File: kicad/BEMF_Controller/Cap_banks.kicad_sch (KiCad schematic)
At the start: 60 parts

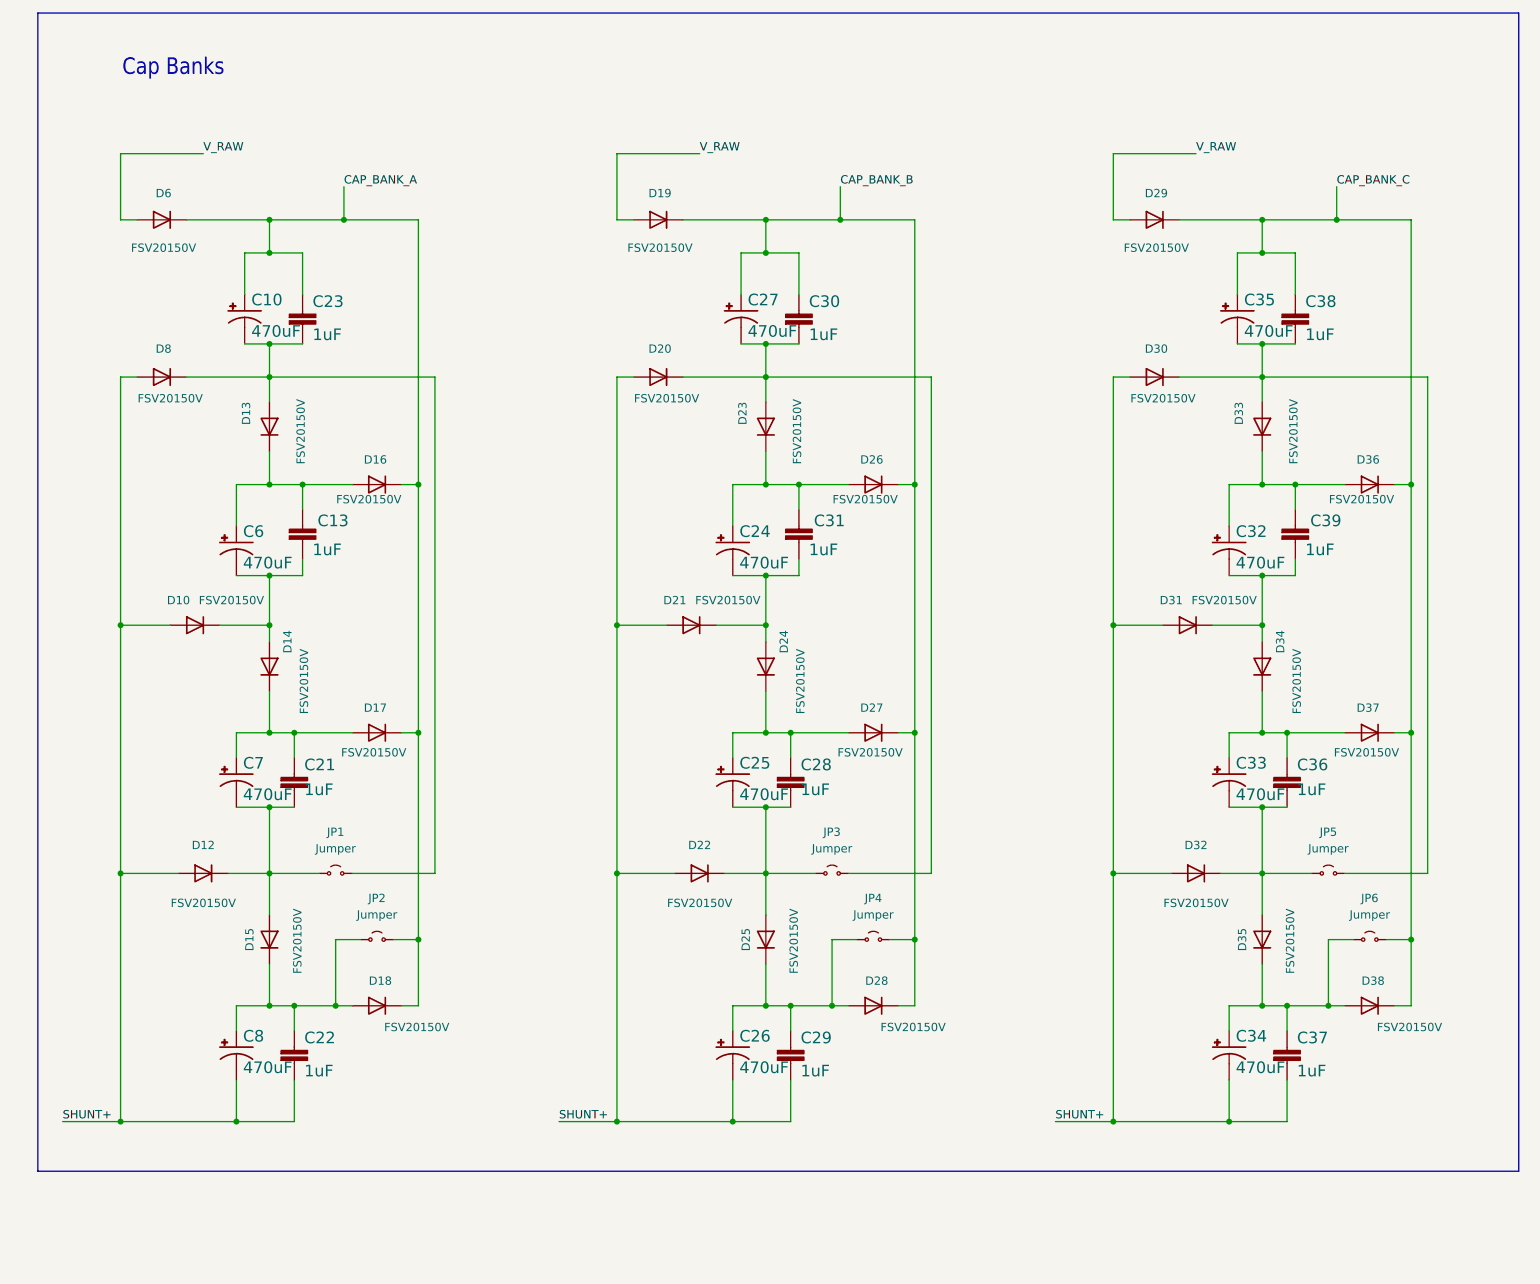
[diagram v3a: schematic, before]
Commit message: Updated Shottky footprint
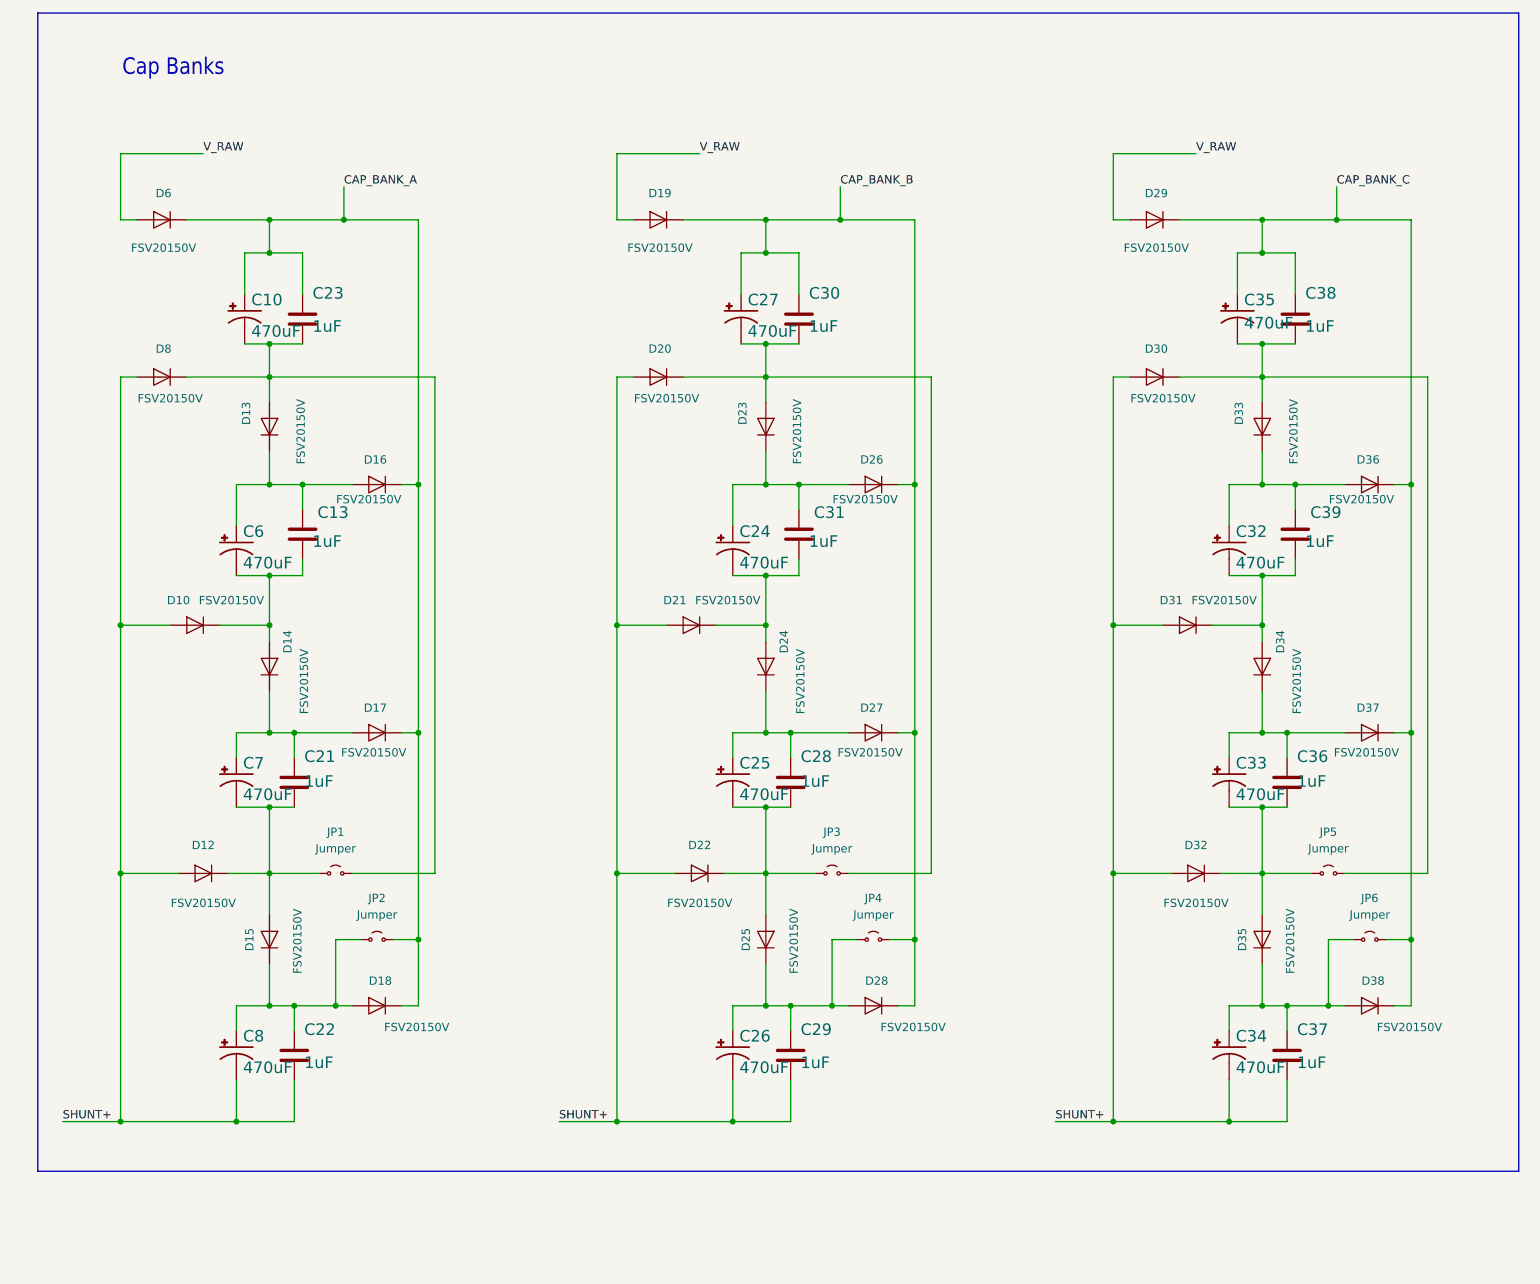
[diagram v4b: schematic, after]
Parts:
- C13, C21, C22, C23, C28, C29, C30, C31, C36, C37, C38, C39: footprint main:1206 -> Capacitor_SMD:C_1812_4532Metric; symbol main-eagle-import:1.0UF-1206-50V-10% -> Component_Library:CHV1812N250105MXT
- D10, D12, D13, D14, D15, D16, D17, D18, D19, D20, D21, D22, D23, D24, D25, D26, D27, D28, D29, D30, D31, D32, D33, D34, D35, D36, D37, D38, D6, D8: symbol Device:D -> Component_Library:FSV20150V
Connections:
- net CAP_BANK_A: now also D16.2 (A), D17.2 (A), D18.2 (A), D6.2 (A)
- net CAP_BANK_B: now also D19.2 (A), D26.2 (A), D27.2 (A), D28.2 (A)
- net CAP_BANK_C: now also D29.2 (A), D36.2 (A), D37.2 (A), D38.2 (A)
- net SHUNT+: now also D10.3 (K), D12.3 (K), D20.3 (K), D21.3 (K), D22.3 (K), D30.3 (K), D31.3 (K), D32.3 (K), D8.3 (K); no longer D10.2 (A), D12.2 (A), D20.2 (A), D21.2 (A), D22.2 (A), D30.2 (A), D31.2 (A), D32.2 (A), D8.2 (A)
- net V_RAW: now also D19.3 (K), D29.3 (K), D6.3 (K); no longer D19.2 (A), D29.2 (A), D6.2 (A)
- net at C27.-, C30.2, D20.1 (A)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: now also D20.2 (A), D23.3 (K); no longer D23.2 (A)
- net at C25.+, C28.1, D24.1 (A): now also D24.2 (A), D27.3 (K); no longer D27.2 (A)
- net at C24.-, C31.2, D21.1 (A): now also D21.2 (A), D24.3 (K); no longer D24.2 (A)
- net at C13.1, C6.+, D13.1 (A): now also D13.2 (A), D16.3 (K); no longer D16.2 (A)
- net at C34.+, C37.1, D35.1 (A)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: now also D35.2 (A), D38.3 (K); no longer D38.2 (A)
- net at C10.-, C23.2, D8.1 (A)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: now also D13.3 (K), D8.2 (A); no longer D13.2 (A)
- net at C22.1, C8.+, D15.1 (A)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: now also D15.2 (A), D18.3 (K); no longer D18.2 (A)
- net at C26.+, C29.1, D25.1 (A)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: now also D25.2 (A), D28.3 (K); no longer D28.2 (A)
- net at C25.-, C28.2, D22.1 (A)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: now also D22.2 (A), D25.3 (K); no longer D25.2 (A)
- net at C33.+, C36.1, D34.1 (A): now also D34.2 (A), D37.3 (K); no longer D37.2 (A)
- net at C33.-, C36.2, D32.1 (A)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: now also D32.2 (A), D35.3 (K); no longer D35.2 (A)
- net at C21.2, C7.-, D12.1 (A)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: now also D12.2 (A), D15.3 (K); no longer D15.2 (A)
- net at C35.-, C38.2, D30.1 (A)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: now also D30.2 (A), D33.3 (K); no longer D33.2 (A)
- net at C13.2, C6.-, D10.1 (A): now also D10.2 (A), D14.3 (K); no longer D14.2 (A)
- net at C24.+, C31.1, D23.1 (A): now also D23.2 (A), D26.3 (K); no longer D26.2 (A)
- net at C32.+, C39.1, D33.1 (A): now also D33.2 (A), D36.3 (K); no longer D36.2 (A)
- net at C21.1, C7.+, D14.1 (A): now also D14.2 (A), D17.3 (K); no longer D17.2 (A)
- net at C32.-, C39.2, D31.1 (A): now also D31.2 (A), D34.3 (K); no longer D34.2 (A)

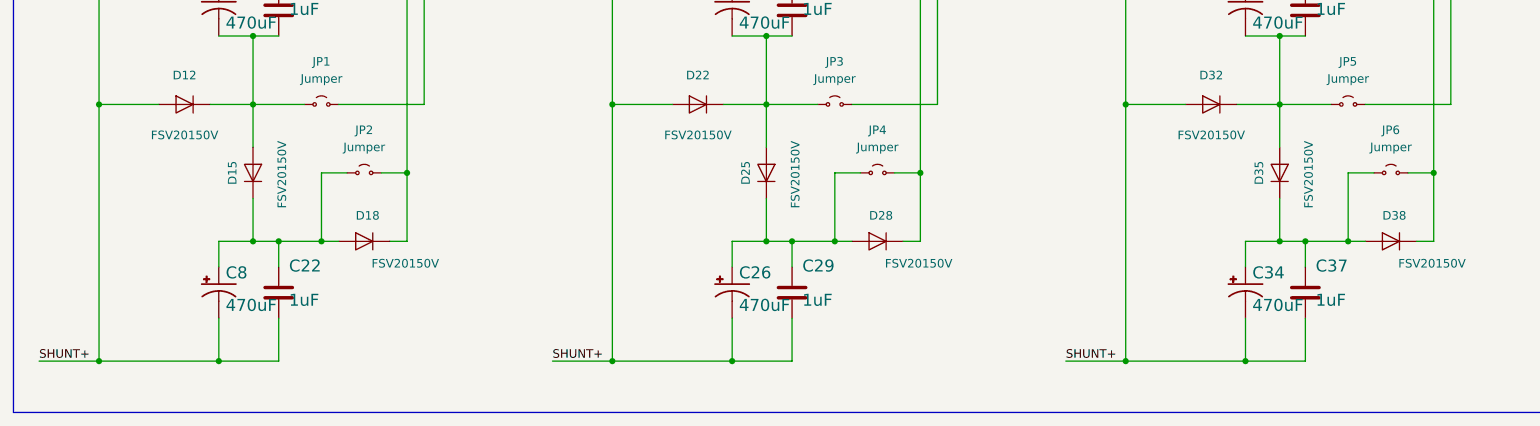
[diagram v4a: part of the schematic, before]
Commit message: Added external spi ADC for current and voltage sense per bridge
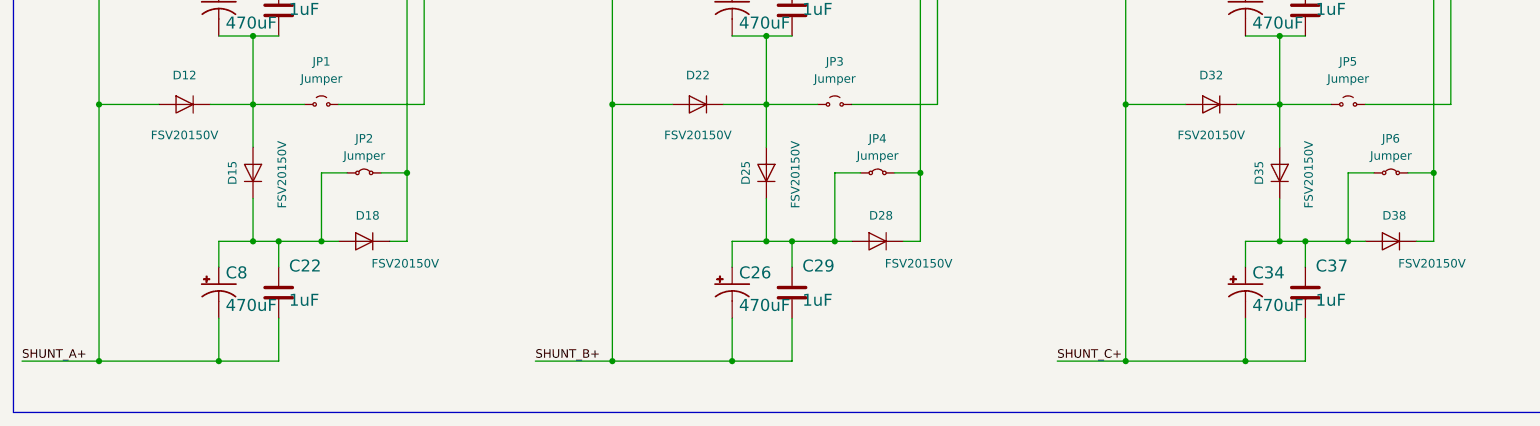
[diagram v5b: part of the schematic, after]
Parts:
- removed JP2, JP4, JP6: Jumper, Jumper:SolderJumper-2_P1.3mm_Open_RoundedPad1.0x1.5mm, symbol Jumper:Jumper_2_Small_Open
- added JP2, JP4, JP6: Jumper, Jumper:SolderJumper-2_P1.3mm_Bridged2Bar_RoundedPad1.0x1.5mm, symbol Jumper:Jumper_2_Small_Bridged
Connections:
- net CAP_BANK_A: now also JP2.2 (B)
- net CAP_BANK_B: now also JP4.2 (B)
- net CAP_BANK_C: now also JP6.2 (B)
- net at C34.+, C37.1, D35.1 (A)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: now also JP6.1 (A)
- net at C22.1, C8.+, D15.1 (A)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: now also JP2.1 (A)
- net at C26.+, C29.1, D25.1 (A)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: now also JP4.1 (A)
- removed net SHUNT+: C22.2, C26.-, C29.2, C34.-, C37.2, C8.-, D10.3 (K), D12.3 (K), D20.3 (K), D21.3 (K), D22.3 (K), D30.3 (K), D31.3 (K), D32.3 (K), D8.3 (K)
- new net SHUNT_A+: C22.2, C8.-, D10.3 (K), D12.3 (K), D8.3 (K)
- new net SHUNT_B+: C26.-, C29.2, D20.3 (K), D21.3 (K), D22.3 (K)
- new net SHUNT_C+: C34.-, C37.2, D30.3 (K), D31.3 (K), D32.3 (K)
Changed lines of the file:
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@@
 	(wire
 		(pts
-			(xy 12.7 175.26) (xy 21.59 175.26)
+			(xy 10.16 175.26) (xy 21.59 175.26)
 		)
 		(stroke
@@
 	(wire
 		(pts
-			(xy 88.9 175.26) (xy 97.79 175.26)
+			(xy 86.36 175.26) (xy 97.79 175.26)
 		)
 		(stroke
@@
 	(wire
 		(pts
-			(xy 165.1 175.26) (xy 173.99 175.26)
+			(xy 163.83 175.26) (xy 173.99 175.26)
 		)
 		(stroke
@@
 		)
 	)
-	(label "SHUNT+"
-		(at 88.9 175.26 0)
+	(label "SHUNT_B+"
+		(at 86.36 175.26 0)
 		(fields_autoplaced yes)
 		(effects
@@
 		)
 	)
-	(label "SHUNT+"
-		(at 165.1 175.26 0)
+	(label "SHUNT_C+"
+		(at 163.83 175.26 0)
 		(fields_autoplaced yes)
 		(effects
@@
 		)
 	)
-	(label "SHUNT+"
-		(at 12.7 175.26 0)
+	(label "SHUNT_A+"
+		(at 10.16 175.26 0)
 		(fields_autoplaced yes)
 		(effects
@@
 	)
 	(symbol
-		(lib_id "Jumper:Jumper_2_Small_Open")
-		(at 213.36 147.32 0)
-		(unit 1)
-		(exclude_from_sim yes)
-		(in_bom yes)
-		(on_board yes)
-		(dnp no)
-		(fields_autoplaced yes)
-		(property "Reference" "JP6"
-			(at 213.36 140.97 0)
-			(effects
-				(font
-					(size 1.27 1.27)
-				)
-			)
-		)
-		(property "Value" "Jumper"
-			(at 213.36 143.51 0)
-			(effects
-				(font
-					(size 1.27 1.27)
-				)
-			)
-		)
-		(property "Footprint" "Jumper:SolderJumper-2_P1.3mm_Open_RoundedPad1.0x1.5mm"
-			(at 213.36 147.32 0)
-			(effects
-				(font
-					(size 1.27 1.27)
-				)
-				(hide yes)
-			)
-		)
-		(property "Datasheet" "~"
-			(at 213.36 147.32 0)
-			(effects
-				(font
-					(size 1.27 1.27)
-				)
-				(hide yes)
-			)
-		)
-		(property "Description" "Jumper, 2-pole, small symbol, open"
-			(at 213.36 147.32 0)
-			(effects
-				(font
-					(size 1.27 1.27)
-				)
-				(hide yes)
-			)
-		)
-		(pin "1"
-		)
-		(pin "2"
-		)
-		(instances
-			(project "BEMF_Controller"
-				(path "/80a514a6-29a9-4699-8a7d-cff678a7ed07/6cedb8d4-aa7c-4752-8b92-b860036c6340"
-					(reference "JP6")
-					(unit 1)
-				)
-			)
-		)
-	)
-	(symbol
 		(lib_id "Component_Library:FSV20150V")
 		(at 44.45 68.58 270)
@@
 	)
 	(symbol
+		(lib_id "Jumper:Jumper_2_Small_Bridged")
+		(at 60.96 147.32 0)
+		(unit 1)
+		(exclude_from_sim yes)
+		(in_bom yes)
+		(on_board yes)
+		(dnp no)
+		(fields_autoplaced yes)
+		(property "Reference" "JP2"
+			(at 60.96 142.24 0)
+			(effects
+				(font
+					(size 1.27 1.27)
+				)
+			)
+		)
+		(property "Value" "Jumper"
+			(at 60.96 144.78 0)
+			(effects
+				(font
+					(size 1.27 1.27)
+				)
+			)
+		)
+		(property "Footprint" "Jumper:SolderJumper-2_P1.3mm_Bridged2Bar_RoundedPad1.0x1.5mm"
+			(at 60.96 147.32 0)
+			(effects
+				(font
+					(size 1.27 1.27)
+				)
+				(hide yes)
+			)
+		)
+		(property "Datasheet" "~"
+			(at 60.96 147.32 0)
+			(effects
+				(font
+					(size 1.27 1.27)
+				)
+				(hide yes)
+			)
+		)
+		(property "Description" "Jumper, 2-pole, small symbol, bridged"
+			(at 60.96 147.32 0)
+			(effects
+				(font
+					(size 1.27 1.27)
+				)
+				(hide yes)
+			)
+		)
+		(pin "1"
+		)
+		(pin "2"
+		)
+		(instances
+			(project ""
+				(path "/80a514a6-29a9-4699-8a7d-cff678a7ed07/6cedb8d4-aa7c-4752-8b92-b860036c6340"
+					(reference "JP2")
+					(unit 1)
+				)
+			)
+		)
+	)
+	(symbol
 		(lib_id "main-eagle-import:1000UF-RADIAL-5MM-25V-20%")
 		(at 39.37 86.36 0)
@@
 	)
 	(symbol
+		(lib_id "Jumper:Jumper_2_Small_Bridged")
+		(at 213.36 147.32 0)
+		(unit 1)
+		(exclude_from_sim yes)
+		(in_bom yes)
+		(on_board yes)
+		(dnp no)
+		(fields_autoplaced yes)
+		(property "Reference" "JP6"
+			(at 213.36 142.24 0)
+			(effects
+				(font
+					(size 1.27 1.27)
+				)
+			)
+		)
+		(property "Value" "Jumper"
+			(at 213.36 144.78 0)
+			(effects
+				(font
+					(size 1.27 1.27)
+				)
+			)
+		)
+		(property "Footprint" "Jumper:SolderJumper-2_P1.3mm_Bridged2Bar_RoundedPad1.0x1.5mm"
+			(at 213.36 147.32 0)
+			(effects
+				(font
+					(size 1.27 1.27)
+				)
+				(hide yes)
+			)
+		)
+		(property "Datasheet" "~"
+			(at 213.36 147.32 0)
+			(effects
+				(font
+					(size 1.27 1.27)
+				)
+				(hide yes)
+			)
+		)
+		(property "Description" "Jumper, 2-pole, small symbol, bridged"
+			(at 213.36 147.32 0)
+			(effects
+				(font
+					(size 1.27 1.27)
+				)
+				(hide yes)
+			)
+		)
+		(pin "1"
+		)
+		(pin "2"
+		)
+		(instances
+			(project "BEMF_Controller"
+				(path "/80a514a6-29a9-4699-8a7d-cff678a7ed07/6cedb8d4-aa7c-4752-8b92-b860036c6340"
+					(reference "JP6")
+					(unit 1)
+				)
+			)
+		)
+	)
+	(symbol
 		(lib_id "Component_Library:FSV20150V")
 		(at 44.45 105.41 270)
@@
 	)
 	(symbol
-		(lib_id "Jumper:Jumper_2_Small_Open")
+		(lib_id "Jumper:Jumper_2_Small_Bridged")
 		(at 137.16 147.32 0)
 		(unit 1)
@@
 		(fields_autoplaced yes)
 		(property "Reference" "JP4"
-			(at 137.16 140.97 0)
+			(at 137.16 142.24 0)
 			(effects
 				(font
@@
 		)
 		(property "Value" "Jumper"
-			(at 137.16 143.51 0)
+			(at 137.16 144.78 0)
 			(effects
 				(font
@@
 			)
 		)
-		(property "Footprint" "Jumper:SolderJumper-2_P1.3mm_Open_RoundedPad1.0x1.5mm"
+		(property "Footprint" "Jumper:SolderJumper-2_P1.3mm_Bridged2Bar_RoundedPad1.0x1.5mm"
 			(at 137.16 147.32 0)
 			(effects
@@
 			)
 		)
-		(property "Description" "Jumper, 2-pole, small symbol, open"
+		(property "Description" "Jumper, 2-pole, small symbol, bridged"
 			(at 137.16 147.32 0)
 			(effects
@@
 					(unit 1)
 				)
-			)
-		)
-	)
-	(symbol
-		(lib_id "Jumper:Jumper_2_Small_Open")
-		(at 60.96 147.32 0)
-		(unit 1)
-		(exclude_from_sim yes)
-		(in_bom yes)
-		(on_board yes)
-		(dnp no)
-		(fields_autoplaced yes)
-		(property "Reference" "JP2"
-			(at 60.96 140.97 0)
-			(effects
-				(font
-					(size 1.27 1.27)
-				)
-			)
-		)
-		(property "Value" "Jumper"
-			(at 60.96 143.51 0)
-			(effects
-				(font
-					(size 1.27 1.27)
-				)
-			)
-		)
-		(property "Footprint" "Jumper:SolderJumper-2_P1.3mm_Open_RoundedPad1.0x1.5mm"
-			(at 60.96 147.32 0)
-			(effects
-				(font
-					(size 1.27 1.27)
-				)
-				(hide yes)
-			)
-		)
-		(property "Datasheet" "~"
-			(at 60.96 147.32 0)
-			(effects
-				(font
-					(size 1.27 1.27)
-				)
-				(hide yes)
-			)
-		)
-		(property "Description" "Jumper, 2-pole, small symbol, open"
-			(at 60.96 147.32 0)
-			(effects
-				(font
-					(size 1.27 1.27)
-				)
-				(hide yes)
-			)
-		)
-		(pin "1"
-		)
-		(pin "2"
-		)
-		(instances
-			(project "BEMF_Controller"
-				(path "/80a514a6-29a9-4699-8a7d-cff678a7ed07/6cedb8d4-aa7c-4752-8b92-b860036c6340"
-					(reference "JP2")
-					(unit 1)
-				)
